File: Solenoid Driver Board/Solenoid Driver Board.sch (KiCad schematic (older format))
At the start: 1 part

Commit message: Initial schematic work
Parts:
- added C?: 100 uF, symbol C
- added C?: 470 nF, symbol C
- added C? (x2): C, symbol C
- added D?: 1N4007, Diodes_THT:D_DO-41_SOD81_Horizontal_RM10, symbol 1N4007
- added J?: DEBUG, symbol CONN_01X04
- added J?: MAIN, symbol CONN_01X03
- added M?: Solenoid, symbol Motor_DC
- added Q?: IRLB8721PBF, TO_SOT_Packages_THT:TO-220_Vertical, symbol IRLB8721PBF
- added R?: 10K, symbol R
- added U?: AMS1117-5.0, TO_SOT_Packages_SMD:SOT-223, symbol AMS1117-5.0
- added Y?: Crystal, symbol Crystal
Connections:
- net FOUNTAIN: now reaches U?.13 ([TIM1_CH1N]TIM1_CH3/PC3)
- net FOUNTAIN: now also Q?.1 (G), R?.2
- net SWIM: now reaches U?.18 (PD1/SWIM)
- net SWIM: now also J?.2 (P2)
- net TX: now reaches U?.2 (PD5/AIN5/UART1_TX)
- net RX: now reaches U?.3 (PD6/AIN6/UART1_RX)
- net RX: now also J?.1 (P1)
- net RST: now reaches U?.4 (NRST)
- net RST: now also J?.4 (P4)
- net at U?.5 (OSCIN/PA1): now also C?.2, Y?.1
- net at U?.6 (OSCOUT/PA2): now also C?.2, Y?.2
- net GND: now reaches U?.7 (VSS)
- net GND: now also C?.1, C?.1, C?.2, C?.2, J?.3 (P3), J?.3 (P3), Q?.3 (S), R?.1, U?.1 (GND/ADJ)
- net at U?.8 (Vcap): now also C?.1
- net +5V: now reaches U?.9 (VDD)
- net +5V: now also C?.1, J?.1 (P1), U?.2 (VO), U?.4 (VO)
- new net: D?.2 (A), M?.2 (-), Q?.2 (D)
- new net +12V: D?.1 (K), J?.2 (P2), M?.1 (+), U?.3 (VI)
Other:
- note added: "Optional - External OSC"
- note added: "Solenoid Control"

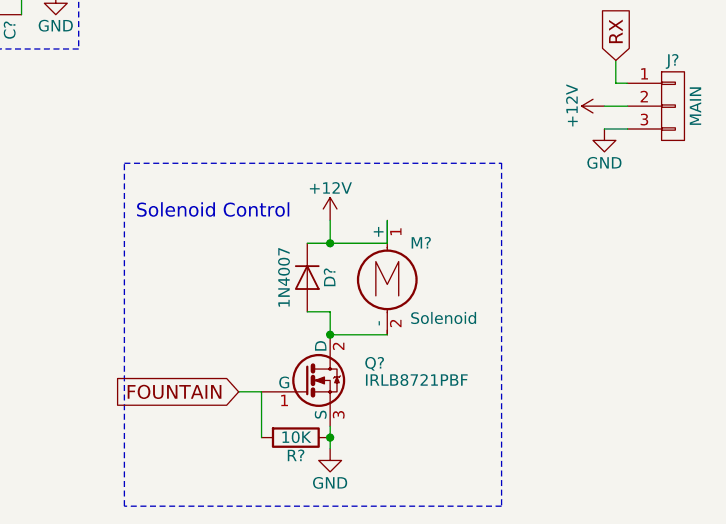
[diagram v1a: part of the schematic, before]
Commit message: Spade connectors added
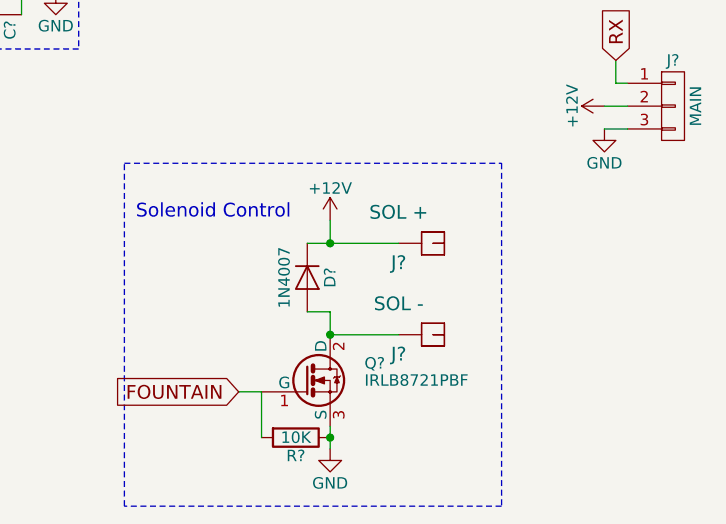
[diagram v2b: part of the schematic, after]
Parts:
- removed M?: Solenoid, symbol Motor_DC
- added J?: SOL +, symbol SPADE
- added J?: SOL -, symbol SPADE
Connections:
- net +12V: now also J?.1
- net at D?.2 (A), Q?.2 (D): now also J?.1
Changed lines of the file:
@@
 	3850 2800 3900 2800
 Wire Wire Line
-	8650 3250 9000 3250
+	8650 3250 9050 3250
 Wire Wire Line
 	8750 3250 8750 3150
@@
 Wire Wire Line
 	8750 3550 8750 3650
-$Comp
-L Motor_DC M?
-U 1 1 58F59024
-P 9000 3350
-F 0 "M?" H 9100 3450 50  0000 L CNN
-F 1 "Solenoid" H 9100 3150 50  0000 L TNN
-F 2 "" H 9000 3260 50  0001 C CNN
-F 3 "" H 9000 3260 50  0001 C CNN
-	1    9000 3350
-	1    0    0    -1
-$EndComp
-Wire Wire Line
-	9000 3250 9000 3150
 Connection ~ 8750 3250
 Wire Wire Line
-	8750 3650 9000 3650
+	8750 3650 9050 3650
 Connection ~ 8750 3650
 Wire Notes Line
@@
 Text Notes 7900 3150 0    60   ~ 0
 Solenoid Control
+$Comp
+L SPADE J?
+U 1 1 58F58731
+P 9150 3250
+F 0 "J?" H 9050 3200 60  0000 C TNN
+F 1 "SOL +" H 9050 3350 60  0000 C BNN
+F 2 "" H 9050 3350 60  0001 C CNN
+F 3 "" H 9050 3350 60  0001 C CNN
+	1    9150 3250
+	1    0    0    -1
+$EndComp
+$Comp
+L SPADE J?
+U 1 1 58F5876D
+P 9150 3650
+F 0 "J?" H 9050 3600 60  0000 C TNN
+F 1 "SOL -" H 9050 3750 60  0000 C BNN
+F 2 "" H 9050 3750 60  0001 C CNN
+F 3 "" H 9050 3750 60  0001 C CNN
+	1    9150 3650
+	1    0    0    -1
+$EndComp
 $EndSCHEMATC
